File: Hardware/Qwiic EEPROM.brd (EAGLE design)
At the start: 25.4 x 25.4 mm, 60 parts, among them J2 QWIIC_RA, J4 QWIIC_RA, U1 RM24C512C

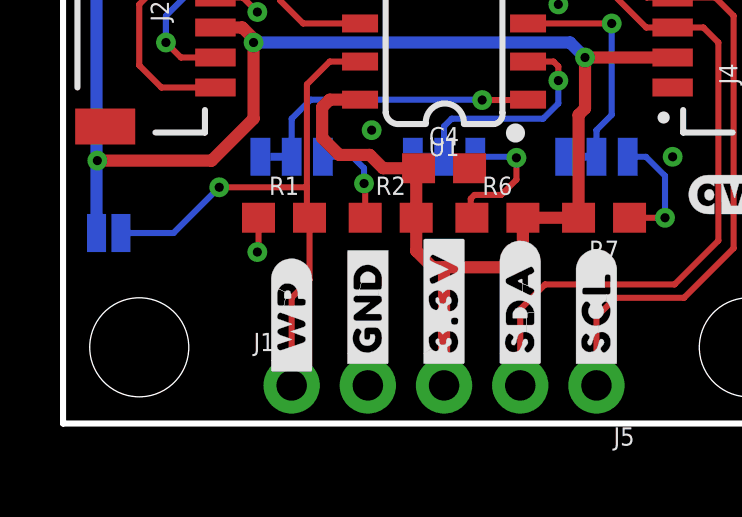
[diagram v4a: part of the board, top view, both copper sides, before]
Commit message: QC Double-check: update silkscreen
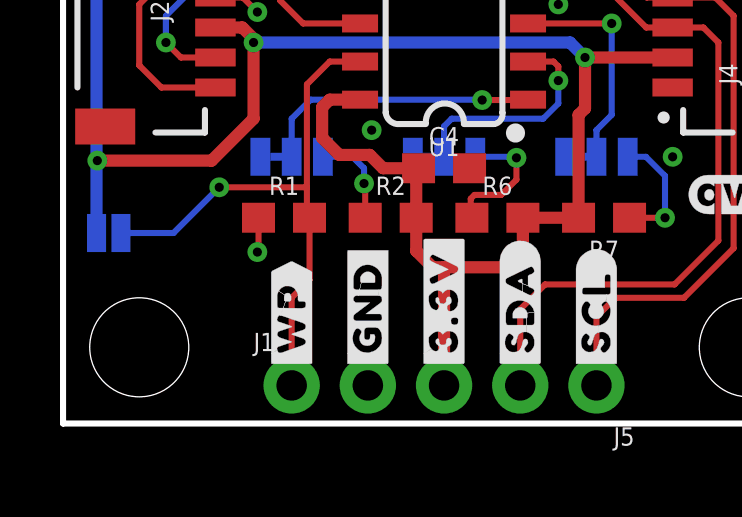
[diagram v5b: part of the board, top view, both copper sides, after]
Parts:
- U$1, U$2: device output:#_WP#0 -> output:#WP#1
- U$18: device output:#PWR#0 -> output:#LED#2
- moved U$18 0.52 mm to (7.62, 19.1)
- moved U$1 0.25 mm to (7.62, 1.65)
- moved U$2 0.25 mm to (7.62, 1.65)
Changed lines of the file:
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@@
 <?xml version="1.0" encoding="utf-8"?>
 <!DOCTYPE eagle SYSTEM "eagle.dtd">
-<eagle version="9.5.2">
+<eagle version="9.6.2">
 <drawing>
 <settings>
@@
 <element name="U$22" library="output" package="10" value="" x="9.652" y="6.985" smashed="yes" rot="MR0"/>
 <element name="U$12" library="output" package="PWR0" value="" x="0" y="17.399" smashed="yes"/>
-<element name="U$18" library="output" package="#PWR#0" value="" x="8.128" y="18.923" smashed="yes" rot="MR0"/>
 <element name="U$19" library="output" package="QWIIC_EEPROM0" value="" x="6.858" y="23.495" smashed="yes"/>
 <element name="U$20" library="output" package="QWIIC_EEPROM0" value="" x="18.669" y="23.495" smashed="yes" rot="MR0"/>
@@
 <element name="U$24" library="output" package="BREAKOUT_#_512KBIT0" value="" x="20.066" y="22.225" smashed="yes" rot="MR0"/>
 <element name="U$3" library="output" package="#WP#0" value="" x="6.096" y="6.35" smashed="yes" rot="MR0"/>
-<element name="U$1" library="output" package="#_WP#0" value="" x="7.62" y="1.397" smashed="yes" rot="R90"/>
-<element name="U$2" library="output" package="#_WP#0" value="" x="7.62" y="1.397" smashed="yes" rot="MR90"/>
+<element name="U$1" library="output" package="#WP#1" value="" x="7.62" y="1.651" smashed="yes" rot="R90"/>
+<element name="U$2" library="output" package="#WP#1" value="" x="7.62" y="1.651" smashed="yes" rot="MR90"/>
+<element name="U$18" library="output" package="#LED#2" value="" x="7.62" y="19.05" smashed="yes" rot="MR0"/>
 </elements>
 <signals>

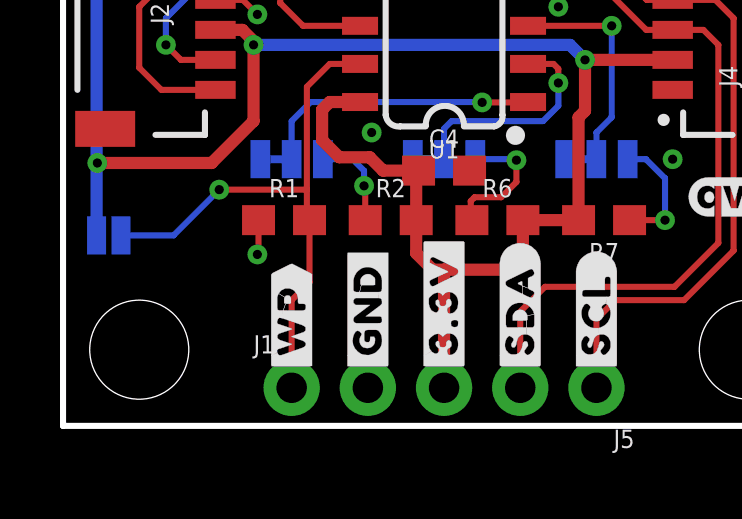
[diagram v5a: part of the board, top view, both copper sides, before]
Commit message: Update WP buzzard label
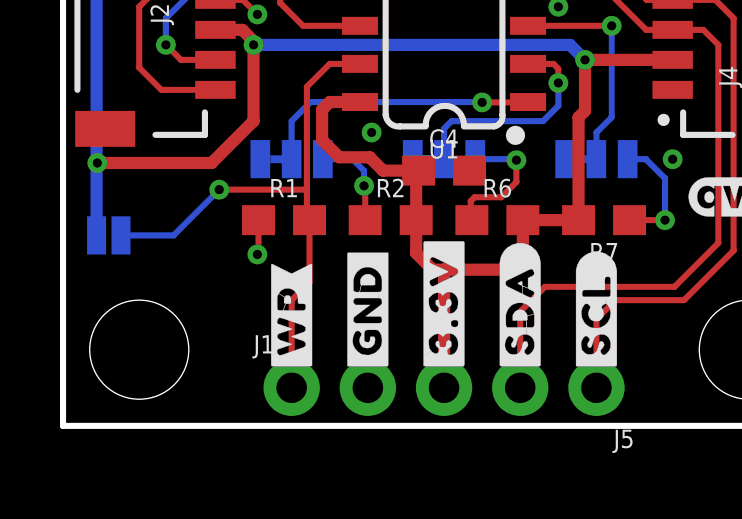
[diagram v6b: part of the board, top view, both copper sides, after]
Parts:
- U$1, U$2: device output:#WP#1 -> output:#WP#3
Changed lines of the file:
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@@
 <drawing>
 <settings>
-<setting alwaysvectorfont="yes"/>
+<setting alwaysvectorfont="no"/>
 <setting keepoldvectorfont="yes"/>
 <setting verticaltext="up"/>
@@
 <element name="U$24" library="output" package="BREAKOUT_#_512KBIT0" value="" x="20.066" y="22.225" smashed="yes" rot="MR0"/>
 <element name="U$3" library="output" package="#WP#0" value="" x="6.096" y="6.35" smashed="yes" rot="MR0"/>
-<element name="U$1" library="output" package="#WP#1" value="" x="7.62" y="1.651" smashed="yes" rot="R90"/>
-<element name="U$2" library="output" package="#WP#1" value="" x="7.62" y="1.651" smashed="yes" rot="MR90"/>
 <element name="U$18" library="output" package="#LED#2" value="" x="7.62" y="19.05" smashed="yes" rot="MR0"/>
+<element name="U$1" library="output" package="#WP#3" value="" x="7.62" y="1.651" smashed="yes" rot="R90"/>
+<element name="U$2" library="output" package="#WP#3" value="" x="7.62" y="1.651" smashed="yes" rot="MR90"/>
 </elements>
 <signals>
